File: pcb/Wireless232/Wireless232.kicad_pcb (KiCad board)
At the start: 2 copper layers, 61 x 56 mm, 16 parts, among them J1 Power, J2 DTE Connector, J3 DCE Connector, U1 ESP32_DevKitC, U2 MAX202

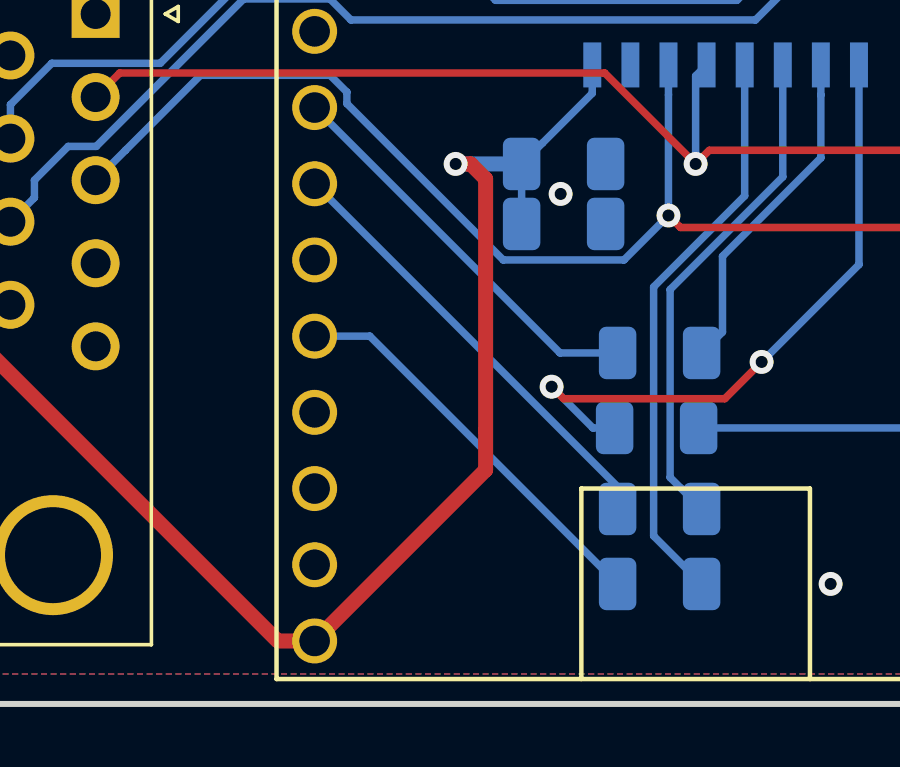
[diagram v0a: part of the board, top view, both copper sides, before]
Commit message: PCB Tidy, improved examples for laser monitoring
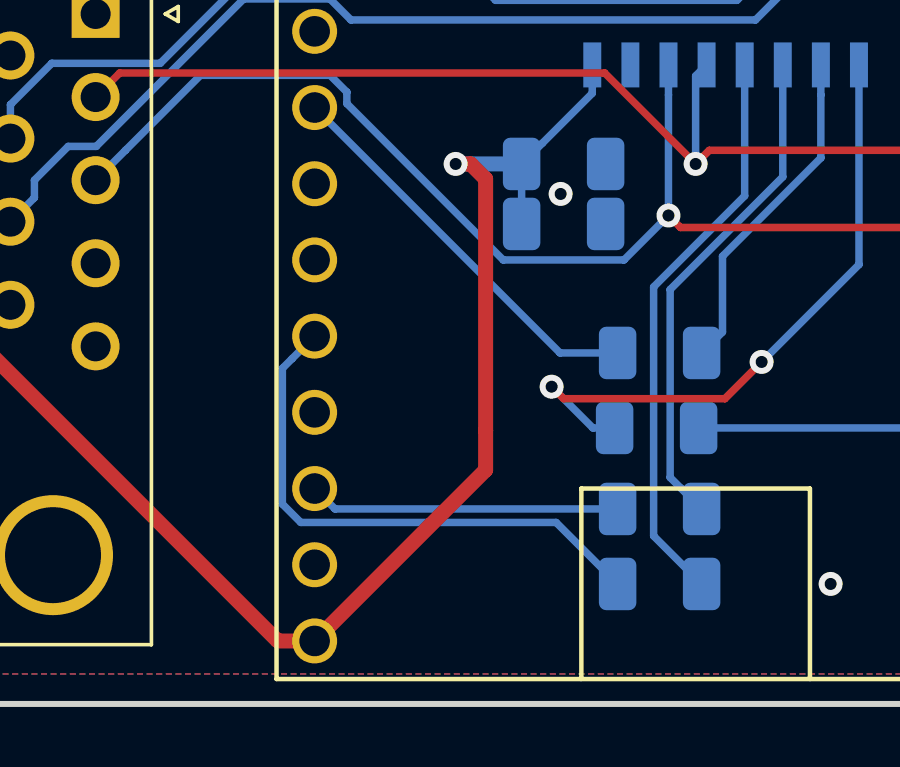
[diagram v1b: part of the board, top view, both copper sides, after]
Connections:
- R3 pad 2: Net-(R3-Pad2) -> /ESP_TX
- U1 pad 13: Net-(R3-Pad2) -> Net-(U1-Pad13)
- U1 pad 17: Net-(U1-Pad17) -> /ESP_TX
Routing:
- net Net-(R3-Pad2): track 15.0 -> 0.00 mm
- net /ESP_TX: track 0.00 -> 11.1 mm
- net Net-(R1-Pad2): track 13.5 -> 18.3 mm
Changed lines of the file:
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@@
-(kicad_pcb (version 20171130) (host pcbnew 5.0.2+dfsg1-1)
+(kicad_pcb (version 20171130) (host pcbnew 5.0.2-bee76a0~70~ubuntu18.04.1)
   (general
     (thickness 1.6)
     (drawings 13)
-    (tracks 136)
+    (tracks 141)
     (zones 0)
     (modules 16)
@@
   (net 50 "Net-(R2-Pad1)")
   (net 51 "Net-(R3-Pad1)")
-  (net 52 "Net-(R3-Pad2)")
-  (net 53 "Net-(R4-Pad2)")
-  (net 54 "Net-(R4-Pad1)")
-  (net 55 "Net-(U1-Pad20)")
-  (net 56 "Net-(U1-Pad18)")
-  (net 57 "Net-(U1-Pad17)")
-  (net 58 "Net-(U1-Pad16)")
+  (net 52 "Net-(R4-Pad2)")
+  (net 53 "Net-(R4-Pad1)")
+  (net 54 "Net-(U1-Pad20)")
+  (net 55 "Net-(U1-Pad18)")
+  (net 56 "Net-(U1-Pad16)")
+  (net 57 /ESP_TX)
+  (net 58 "Net-(U1-Pad13)")
   (net_class Default "This is the default net class."
     (clearance 0.2)
@@
     (add_net /DSR)
     (add_net /DTR)
+    (add_net /ESP_TX)
     (add_net /RI)
     (add_net /RTS)
@@
     (add_net "Net-(R2-Pad2)")
     (add_net "Net-(R3-Pad1)")
-    (add_net "Net-(R3-Pad2)")
     (add_net "Net-(R4-Pad1)")
     (add_net "Net-(R4-Pad2)")
@@
     (add_net "Net-(U1-Pad10)")
     (add_net "Net-(U1-Pad11)")
+    (add_net "Net-(U1-Pad13)")
     (add_net "Net-(U1-Pad16)")
-    (add_net "Net-(U1-Pad17)")
     (add_net "Net-(U1-Pad18)")
     (add_net "Net-(U1-Pad2)")
@@
       (net 24 "Net-(U1-Pad21)"))
     (pad 20 thru_hole circle (at 12.7 25.4) (size 1.5 1.5) (drill 1.02) (layers *.Cu *.Mask)
-      (net 55 "Net-(U1-Pad20)"))
+      (net 54 "Net-(U1-Pad20)"))
     (pad 19 thru_hole circle (at -12.7 25.4) (size 1.5 1.5) (drill 1.02) (layers *.Cu *.Mask)
       (net 12 +5V))
     (pad 18 thru_hole circle (at -12.7 22.86) (size 1.5 1.5) (drill 1.02) (layers *.Cu *.Mask)
-      (net 56 "Net-(U1-Pad18)"))
+      (net 55 "Net-(U1-Pad18)"))
     (pad 17 thru_hole circle (at -12.7 20.32) (size 1.5 1.5) (drill 1.02) (layers *.Cu *.Mask)
-      (net 57 "Net-(U1-Pad17)"))
+      (net 57 /ESP_TX))
     (pad 16 thru_hole circle (at -12.7 17.78) (size 1.5 1.5) (drill 1.02) (layers *.Cu *.Mask)
-      (net 58 "Net-(U1-Pad16)"))
+      (net 56 "Net-(U1-Pad16)"))
     (pad 15 thru_hole circle (at -12.7 15.24) (size 1.5 1.5) (drill 1.02) (layers *.Cu *.Mask)
       (net 48 "Net-(R1-Pad2)"))
@@
       (net 11 GND))
     (pad 13 thru_hole circle (at -12.7 10.16) (size 1.5 1.5) (drill 1.02) (layers *.Cu *.Mask)
-      (net 52 "Net-(R3-Pad2)"))
+      (net 58 "Net-(U1-Pad13)"))
     (pad 12 thru_hole circle (at -12.7 7.62) (size 1.5 1.5) (drill 1.02) (layers *.Cu *.Mask)
-      (net 53 "Net-(R4-Pad2)"))
+      (net 52 "Net-(R4-Pad2)"))
     (pad 11 thru_hole circle (at -12.7 5.08) (size 1.5 1.5) (drill 1.02) (layers *.Cu *.Mask)
       (net 23 "Net-(U1-Pad11)"))
@@
     (fp_line (start -1.6 -0.8) (end -1.6 0.8) (layer B.Fab) (width 0.1))
     (pad 2 smd roundrect (at 1.4 0 180) (size 1.25 1.75) (layers B.Cu B.Paste B.Mask) (roundrect_rratio 0.2)
-      (net 53 "Net-(R4-Pad2)"))
+      (net 52 "Net-(R4-Pad2)"))
     (pad 1 smd roundrect (at -1.4 0 180) (size 1.25 1.75) (layers B.Cu B.Paste B.Mask) (roundrect_rratio 0.2)
-      (net 54 "Net-(R4-Pad1)"))
+      (net 53 "Net-(R4-Pad1)"))
     (model ${KISYS3DMOD}/Resistor_SMD.3dshapes/R_1206_3216Metric.wrl
       (at (xyz 0 0 0))
@@
       (net 51 "Net-(R3-Pad1)"))
     (pad 2 smd roundrect (at 1.4 0 180) (size 1.25 1.75) (layers B.Cu B.Paste B.Mask) (roundrect_rratio 0.2)
-      (net 52 "Net-(R3-Pad2)"))
+      (net 57 /ESP_TX))
     (model ${KISYS3DMOD}/Resistor_SMD.3dshapes/R_1206_3216Metric.wrl
       (at (xyz 0 0 0))
@@
       (net 50 "Net-(R2-Pad1)"))
     (pad 10 smd rect (at 2.7 -3.175 270) (size 1.5 0.6) (layers B.Cu B.Paste B.Mask)
-      (net 54 "Net-(R4-Pad1)"))
+      (net 53 "Net-(R4-Pad1)"))
     (pad 11 smd rect (at 2.7 -1.905 270) (size 1.5 0.6) (layers B.Cu B.Paste B.Mask)
       (net 51 "Net-(R3-Pad1)"))
@@
   (segment (start 123.6 105.4) (end 125.2 107) (width 0.25) (layer B.Cu) (net 47))
   (segment (start 123.6 97.1) (end 123.6 105.4) (width 0.25) (layer B.Cu) (net 47))
-  (segment (start 114.14 98.74) (end 122.4 107) (width 0.25) (layer B.Cu) (net 48))
-  (segment (start 112.3 98.74) (end 114.14 98.74) (width 0.25) (layer B.Cu) (net 48))
+  (segment (start 111.550001 99.489999) (end 112.3 98.74) (width 0.25) (layer B.Cu) (net 48))
+  (segment (start 111.224999 104.336001) (end 111.224999 99.815001) (width 0.25) (layer B.Cu) (net 48))
+  (segment (start 111.224999 99.815001) (end 111.550001 99.489999) (width 0.25) (layer B.Cu) (net 48))
+  (segment (start 111.839008 104.95001) (end 111.224999 104.336001) (width 0.25) (layer B.Cu) (net 48))
+  (segment (start 120.35001 104.95001) (end 111.839008 104.95001) (width 0.25) (layer B.Cu) (net 48))
+  (segment (start 122.4 107) (end 120.35001 104.95001) (width 0.25) (layer B.Cu) (net 48))
   (segment (start 137.18 101.8) (end 137.7 101.28) (width 0.25) (layer B.Cu) (net 49))
   (segment (start 125.1 101.8) (end 137.18 101.8) (width 0.25) (layer B.Cu) (net 49))
@@
   (segment (start 124.14999 103.44999) (end 124.50429 103.80429) (width 0.25) (layer B.Cu) (net 51))
   (segment (start 127.905 89.7) (end 127.905 93.43141) (width 0.25) (layer B.Cu) (net 51))
-  (segment (start 122.4 103.76) (end 122.4 104.5) (width 0.25) (layer B.Cu) (net 52))
-  (segment (start 112.3 93.66) (end 122.4 103.76) (width 0.25) (layer B.Cu) (net 52))
-  (segment (start 120.48 99.3) (end 112.3 91.12) (width 0.25) (layer B.Cu) (net 53))
-  (segment (start 122.4 99.3) (end 120.48 99.3) (width 0.25) (layer B.Cu) (net 53))
-  (segment (start 125.89571 98.60429) (end 125.89571 96.07711) (width 0.25) (layer B.Cu) (net 54))
-  (segment (start 129.175 90.7) (end 129.175 89.7) (width 0.25) (layer B.Cu) (net 54))
-  (segment (start 129.175 92.79782) (end 129.175 90.7) (width 0.25) (layer B.Cu) (net 54))
-  (segment (start 125.89571 96.07711) (end 129.175 92.79782) (width 0.25) (layer B.Cu) (net 54))
-  (segment (start 125.2 99.3) (end 125.89571 98.60429) (width 0.25) (layer B.Cu) (net 54))
+  (segment (start 122.4 103.76) (end 122.4 104.5) (width 0.25) (layer B.Cu) (net 57))
+  (segment (start 120.48 99.3) (end 112.3 91.12) (width 0.25) (layer B.Cu) (net 52))
+  (segment (start 122.4 99.3) (end 120.48 99.3) (width 0.25) (layer B.Cu) (net 52))
+  (segment (start 125.89571 98.60429) (end 125.89571 96.07711) (width 0.25) (layer B.Cu) (net 53))
+  (segment (start 129.175 90.7) (end 129.175 89.7) (width 0.25) (layer B.Cu) (net 53))
+  (segment (start 129.175 92.79782) (end 129.175 90.7) (width 0.25) (layer B.Cu) (net 53))
+  (segment (start 125.89571 96.07711) (end 129.175 92.79782) (width 0.25) (layer B.Cu) (net 53))
+  (segment (start 125.2 99.3) (end 125.89571 98.60429) (width 0.25) (layer B.Cu) (net 53))
+  (segment (start 112.98 104.5) (end 112.3 103.82) (width 0.25) (layer B.Cu) (net 57))
+  (segment (start 122.4 104.5) (end 112.98 104.5) (width 0.25) (layer B.Cu) (net 57))
   (zone (net 0) (net_name "") (layers F&B.Cu) (hatch edge 0.508)
     (connect_pads (clearance 0.508))
